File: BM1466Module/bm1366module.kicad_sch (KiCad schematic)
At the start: 36 parts, among them J2 Conn_02x10_Odd_Even, U1 25MHz, U2 BM1366_mode1

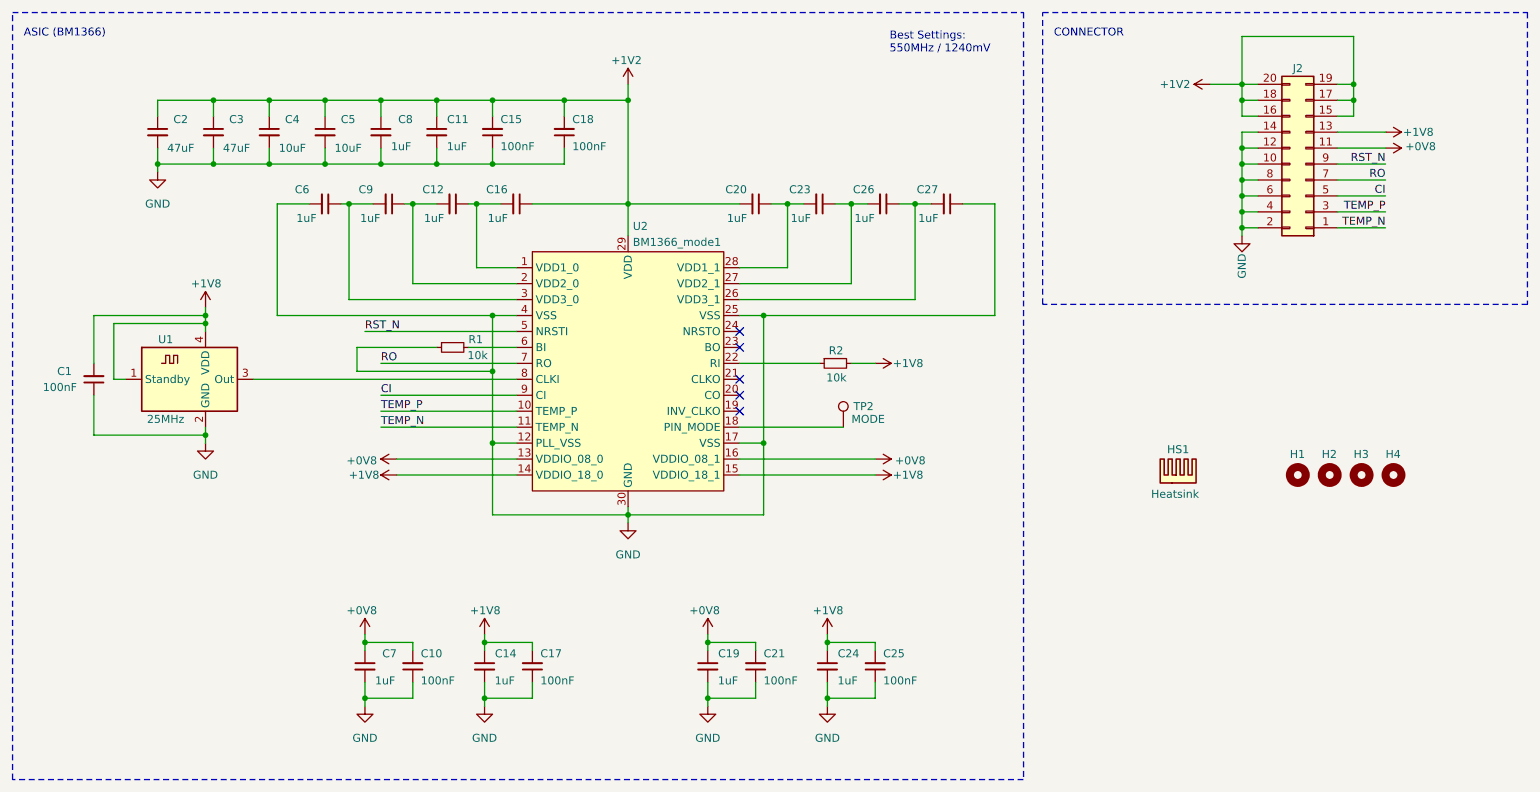
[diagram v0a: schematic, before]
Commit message: Added support for TMP1075 temperature sensor to monitor ASIC
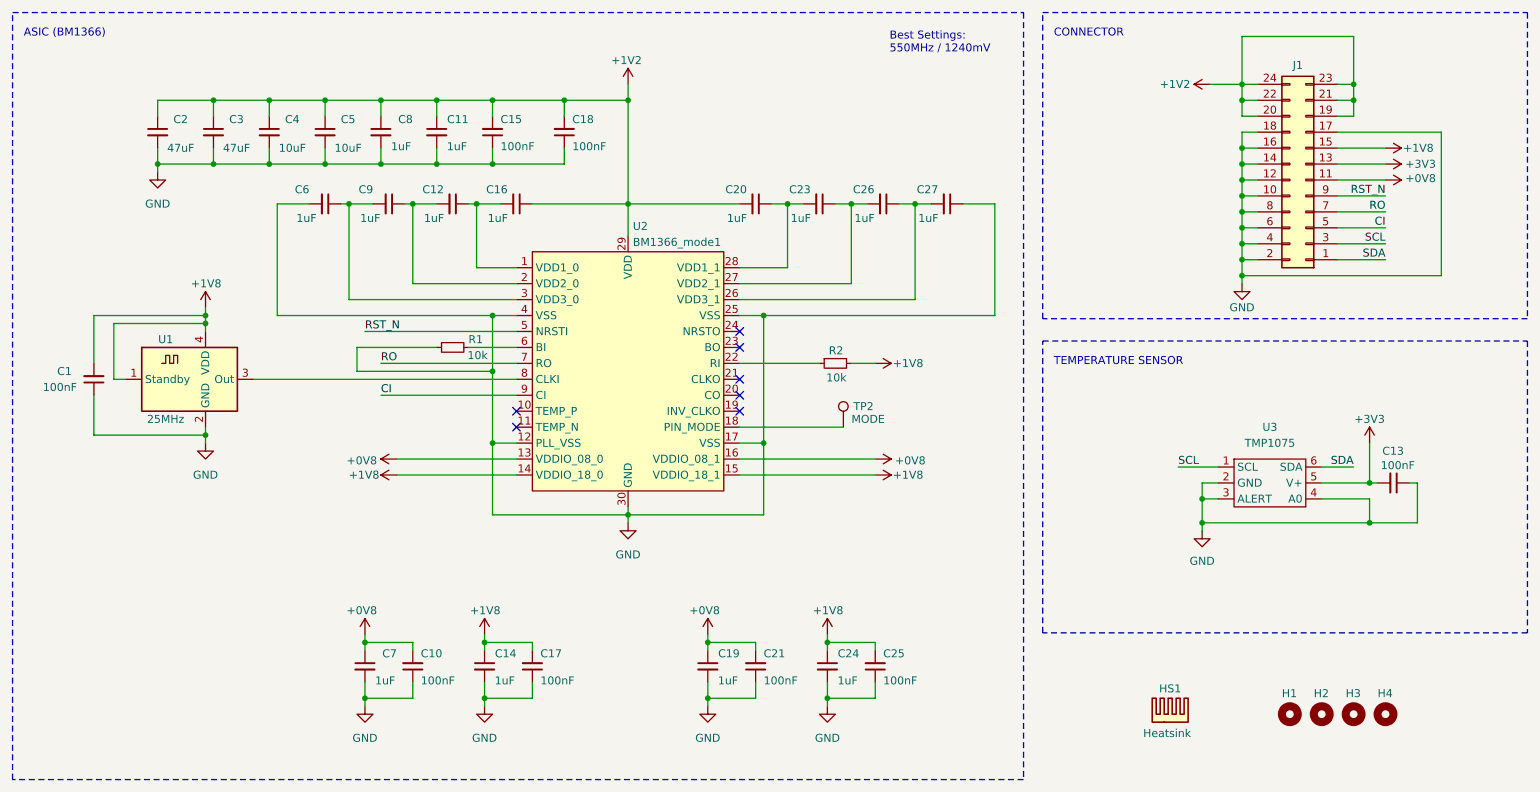
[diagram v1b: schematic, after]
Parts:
- removed J2: Conn_02x10_Odd_Even, Connector_PinSocket_2.54mm:PinSocket_2x10_P2.54mm_Vertical, symbol Connector_Generic:Conn_02x10_Odd_Even
- added C13: 100nF, Capacitor_SMD:C_0603_1608Metric, symbol Device:C_Small
- added J1: Conn_02x12_Odd_Even, Connector_PinSocket_2.54mm:PinSocket_2x12_P2.54mm_Vertical, symbol Connector_Generic:Conn_02x12_Odd_Even
- added U3: TMP1075, Package_TO_SOT_SMD:SOT-563, symbol Sensors_BK:TMP1075
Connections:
- net +0V8: now also J1.11 (Pin_11)
- net +1V2: now also J1.19 (Pin_19), J1.20 (Pin_20), J1.21 (Pin_21), J1.22 (Pin_22), J1.23 (Pin_23), J1.24 (Pin_24)
- net +1V8: now also J1.15 (Pin_15)
- net CI: now also J1.5 (Pin_5)
- net GND: now also C13.1, J1.10 (Pin_10), J1.12 (Pin_12), J1.14 (Pin_14), J1.16 (Pin_16), J1.17 (Pin_17), J1.18 (Pin_18), J1.2 (Pin_2), J1.4 (Pin_4), J1.6 (Pin_6), J1.8 (Pin_8), U3.2 (GND), U3.3 (ALERT), U3.4 (A0)
- net RO: now also J1.7 (Pin_7)
- net RST_N: now also J1.9 (Pin_9)
- net TEMP_N: no longer names the net of U2.11 (TEMP_N)
- net TEMP_P: no longer names the net of U2.10 (TEMP_P)
- new net +3V3: C13.2, J1.13 (Pin_13), U3.5 (V+)
- new net SCL: J1.3 (Pin_3), U3.1 (SCL)
- new net SDA: J1.1 (Pin_1), U3.6 (SDA)
- no-connect marks 5 -> 7
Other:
- note added: "TEMPERATURE SENSOR"
- moved on the sheet: H1, H2, H3, H4, HS1
